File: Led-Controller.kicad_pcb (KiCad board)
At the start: 2 copper layers, 51.3 x 47.1 mm, 62 parts, among them J1 Barrel_Jack, J2 Screw_Terminal, J3 Program, Q1 CSD18540Q5B, Q2 CSD18540Q5B, Q3 CSD18540Q5B, Q4 CSD18540Q5B, Q5 CSD18540Q5B, Q6 CSD18540Q5B, U1 1ED44175N01BXTSA1, U2 1ED44175N01BXTSA1, U3 TPS5430DDA, U4 1ED44175N01BXTSA1, U5 1ED44175N01BXTSA1, U6 TPS5430DDA, U7 1ED44175N01BXTSA1, U8 ESP32-WROOM-32E

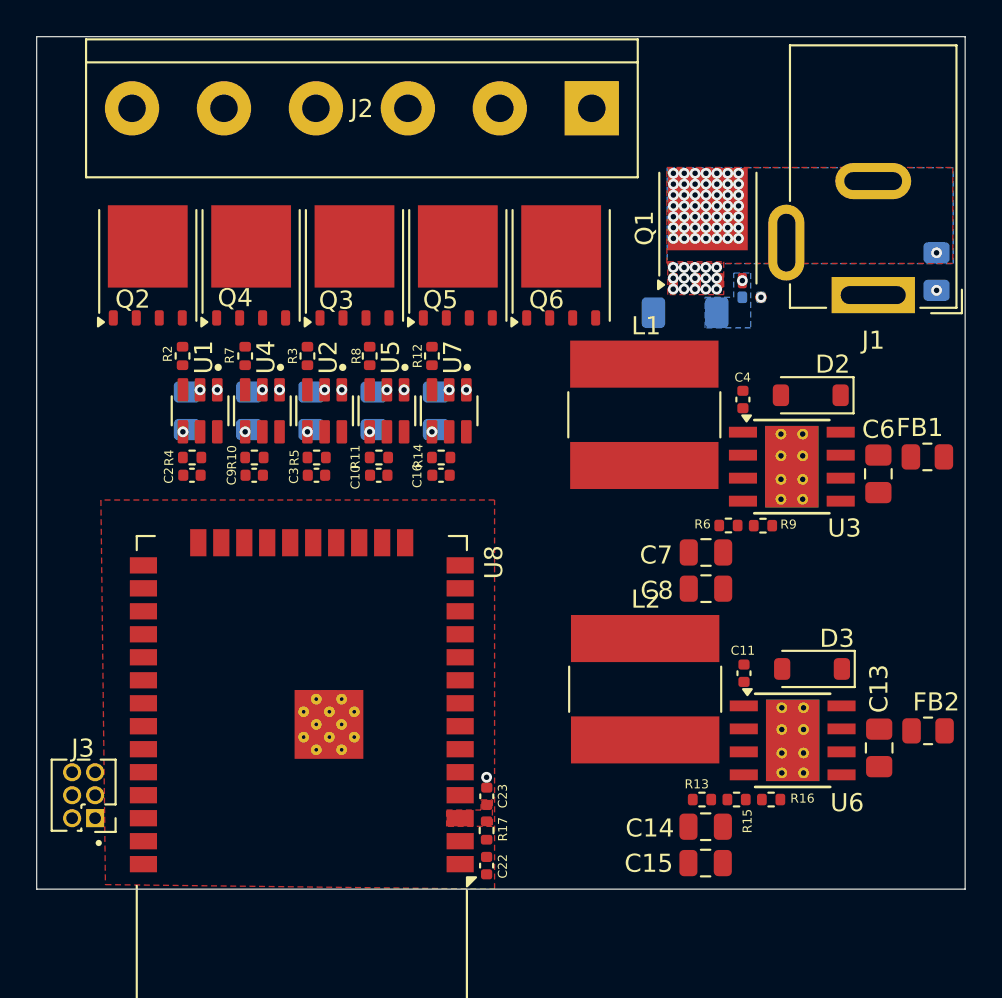
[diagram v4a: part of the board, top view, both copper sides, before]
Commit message: Did basic routing for voltage regulators
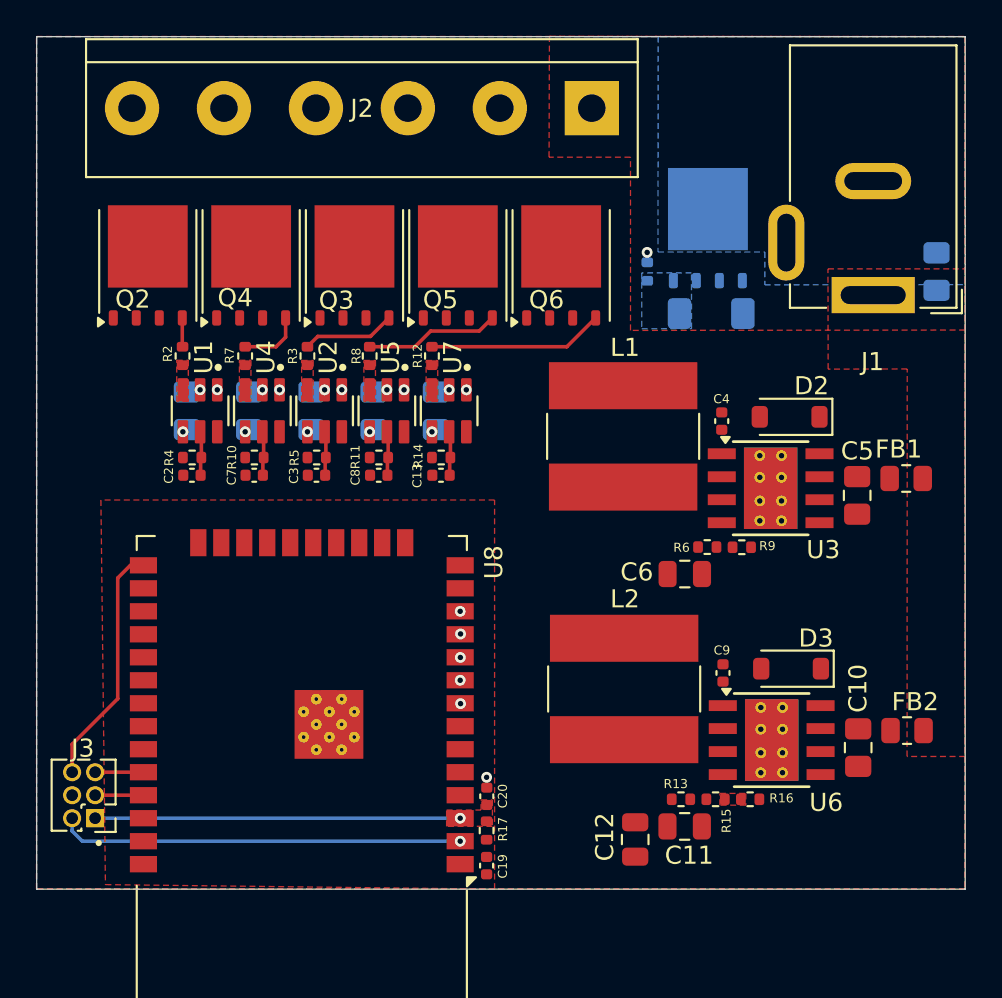
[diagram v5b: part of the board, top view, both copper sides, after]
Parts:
- removed the C8 at (150.5, 90.9)
- Q1: moved to B.Cu
- moved R1 5.93 mm to (147.2, 73.4), turned to 90 degrees
- moved C12 4.10 mm to (146.6, 104.8), turned to 90 degrees
- moved U3 1.67 mm to (154.1, 85.4)
- moved C4 1.67 mm to (151.3, 81.7)
- moved C5 1.67 mm to (158.8, 85.8)
- moved FB1 1.67 mm to (161.5, 84.8)
- moved L1 1.67 mm to (145.9, 82.5)
- moved C6 1.67 mm to (149.3, 90.1)
- moved D2 1.67 mm to (155.1, 81.4)
- moved R6 1.67 mm to (150.6, 88.6), turned to 0 degrees
- moved R9 1.67 mm to (152.5, 88.6)
- moved D1 1.44 mm to (150.8, 75.7), turned to 0 degrees
- moved C10 1.16 mm to (158.9, 99.7)
- moved C9 1.16 mm to (151.4, 95.6)
- moved R16 1.16 mm to (152.9, 102.6)
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- renumbered C13 to C10, C14 to C11, C15 to C12, C16 to C13, C17 to C14, C18 to C15, C19 to C16, C20 to C17, C21 to C18, C22 to C19, C23 to C20, C6 to C5, C7 to C6, C9 to C7, C10 to C8, C11 to C9
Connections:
- U8 pad 11: /IN2 -> /IN4
- U8 pad 12: /IN1 -> /IN5
- U8 pad 8: /IN5 -> /IN1
- U8 pad 9: /IN4 -> /IN2
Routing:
- net +3.3V: track 0.13 -> 22.5 mm, vias 0 -> 1
- net /EN: track 0.24 -> 20.4 mm, vias 0 -> 1
- net /BOOT0: track 0.00 -> 13.5 mm
- net Net-(Q6-G): track 0.00 -> 9.70 mm
- net Net-(Q5-G): track 0.00 -> 7.43 mm
- net Net-(Q3-G): track 0.00 -> 5.16 mm
- net Net-(Q4-G): track 0.00 -> 3.52 mm
- net /TX0: track 0.00 -> 2.67 mm
- net /RX0: track 0.00 -> 2.67 mm
- net Net-(U7-EN/~{FLT}): track 0.00 -> 2.45 mm
- net Net-(U4-EN/~{FLT}): track 0.08 -> 2.53 mm
- net Net-(U5-EN/~{FLT}): track 0.00 -> 2.45 mm
- net Net-(U2-EN/~{FLT}): track 0.06 -> 2.50 mm
- net Net-(U1-EN/~{FLT}): track 0.04 -> 2.49 mm
- net Net-(Q2-G): track 0.00 -> 1.60 mm
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- added copper zone on B.Cu, net GND
- added copper zone on F.Cu, net Net-(R15-Pad2)
- added copper zone on F.Cu, net Net-(U1-OUT)
- added copper zone on F.Cu, net Net-(U2-OUT)
- added copper zone on F.Cu, net Net-(U4-OUT)
- added copper zone on F.Cu, net Net-(U5-OUT)
- added copper zone on F.Cu, net Net-(U7-OUT)
- added copper zone on F.Cu, net VCC
- removed copper zone on F.Cu, net GND1

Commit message: Final Layout of PCB verion 2 alpha
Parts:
- added TP1: ~, TestPoint:TestPoint_Pad_D1.0mm, F.Cu at (140.3, 85.3)
- added TP2: ~, TestPoint:TestPoint_Pad_D1.0mm, F.Cu at (139.9, 105.2)
- added TP3: ~, TestPoint:TestPoint_Pad_D1.0mm, F.Cu at (139.1, 94.7)
- added TP4: ~, TestPoint:TestPoint_Pad_D1.0mm, F.Cu at (139.1, 92.7)
- added TP5: ~, TestPoint:TestPoint_Pad_D1.0mm, F.Cu at (139.1, 90.7)
- added TP6: ~, TestPoint:TestPoint_Pad_D1.0mm, F.Cu at (139.1, 98.8)
- added TP7: ~, TestPoint:TestPoint_Pad_D1.0mm, F.Cu at (139.1, 96.8)
- C14, C15, C16: footprint Capacitor_SMD:C_0805_2012Metric_Pad1.18x1.45mm_HandSolder -> Capacitor_SMD:C_0805_2012Metric
- C19: renamed from C17; footprint Capacitor_SMD:C_0805_2012Metric_Pad1.18x1.45mm_HandSolder -> Capacitor_SMD:C_0805_2012Metric
- C2: renamed from C1; footprint Capacitor_SMD:C_0805_2012Metric_Pad1.18x1.45mm_HandSolder -> Capacitor_SMD:C_0805_2012Metric
- C20: renamed from C18; footprint Capacitor_SMD:C_0805_2012Metric_Pad1.18x1.45mm_HandSolder -> Capacitor_SMD:C_0805_2012Metric
- C3: renamed from C5; footprint Capacitor_SMD:C_0805_2012Metric_Pad1.18x1.45mm_HandSolder -> Capacitor_SMD:C_0805_2012Metric
- C4: renamed from C10; footprint Capacitor_SMD:C_0805_2012Metric_Pad1.18x1.45mm_HandSolder -> Capacitor_SMD:C_0805_2012Metric
- renumbered C19 to C1, C12 to C10, C2 to C11, C7 to C12, C3 to C17, C8 to C18, C20 to C5, C4 to C6, C9 to C7, C11 to C8, C6 to C9, D2 to D1, D3 to D2, D1 to D3, FB2 to FB1, FB1 to FB2, J3 to J1, J1 to J2, J2 to J3, Q4 to Q3, Q6 to Q4, Q3 to Q5, Q5 to Q6, R17 to R1, R14 to R10, R2 to R11, R7 to R12, R12 to R13, R5 to R14, R11 to R15, R3 to R16, R8 to R17, R1 to R2, R6 to R3, R9 to R4, R13 to R5, R15 to R6, R16 to R7, R4 to R8, R10 to R9, U3 to U1, U6 to U2, U8 to U3, U1 to U4, U4 to U5, U7 to U6, U2 to U7, U5 to U8
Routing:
- net /IN1: track 0.11 -> 25.5 mm, vias 1 -> 2
- net /IN2: track 0.03 -> 20.9 mm, vias 1 -> 2
- net /IN3: track 0.01 -> 18.3 mm, vias 1 -> 2
- net /IN4: track 0.03 -> 16.3 mm, vias 1 -> 2
- net /IN5: track 0.00 -> 12.9 mm, vias 1 -> 2
- net +9V: track 0.00 -> 5.57 mm, vias 5 -> 76
- net /BOOT0: track 13.5 -> 14.2 mm
- net GND: vias 11 -> 79
- added copper zone on F.Cu, net +3.3V
- added copper zone on B.Cu, net +9V
- added copper zone on F.Cu, net +9V
- added copper zone on F.Cu, net /OUT1
- added copper zone on F.Cu, net /OUT2
- added copper zone on F.Cu, net /OUT3
- added copper zone on F.Cu, net /OUT4
- added copper zone on F.Cu, net /OUT5
- added copper zone on F.Cu, net Net-(D1-K)
- added copper zone on F.Cu, net Net-(D2-K)
- added copper zone on F.Cu, net Net-(U1-BOOT)
- added copper zone on F.Cu, net Net-(U1-VIN)
- added copper zone on F.Cu, net Net-(U1-VSENSE)
- added copper zone on F.Cu, net Net-(U2-BOOT)
- added copper zone on F.Cu, net Net-(U2-VIN)
- added copper zone on F.Cu, net Net-(U2-VSENSE)
- added copper zone on B.Cu, net VCC
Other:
- board text added: "Made By: Witty Wizard"

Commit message: Added: New Outline file
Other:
- board size 51.3 x 47.1 mm -> 71.3 x 47.1 mm
